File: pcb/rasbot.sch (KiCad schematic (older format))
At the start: 0 parts

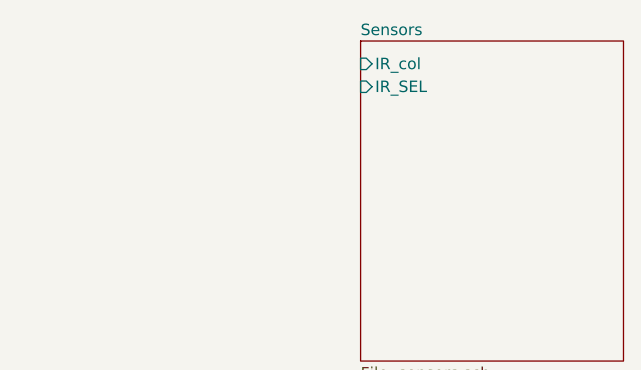
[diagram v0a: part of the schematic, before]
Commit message: IR matrix complete minus control transistor
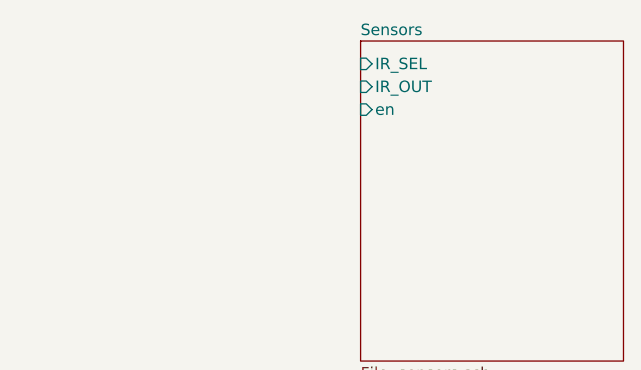
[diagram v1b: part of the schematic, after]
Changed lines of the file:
@@
 $Descr A4 11693 8268
 encoding utf-8
-Sheet 1 19
+Sheet 1 12
 Title ""
 Date ""
@@
 F0 "Sensors" 50
 F1 "sensors.sch" 50
-F2 "IR_col" I L 9200 1300 50
-F3 "IR_SEL" I L 9200 1400 50
+F2 "IR_SEL" I L 9200 1300 50
+F3 "IR_OUT" I L 9200 1400 50
+F4 "en" I L 9200 1500 50
 $EndSheet
 $Sheet

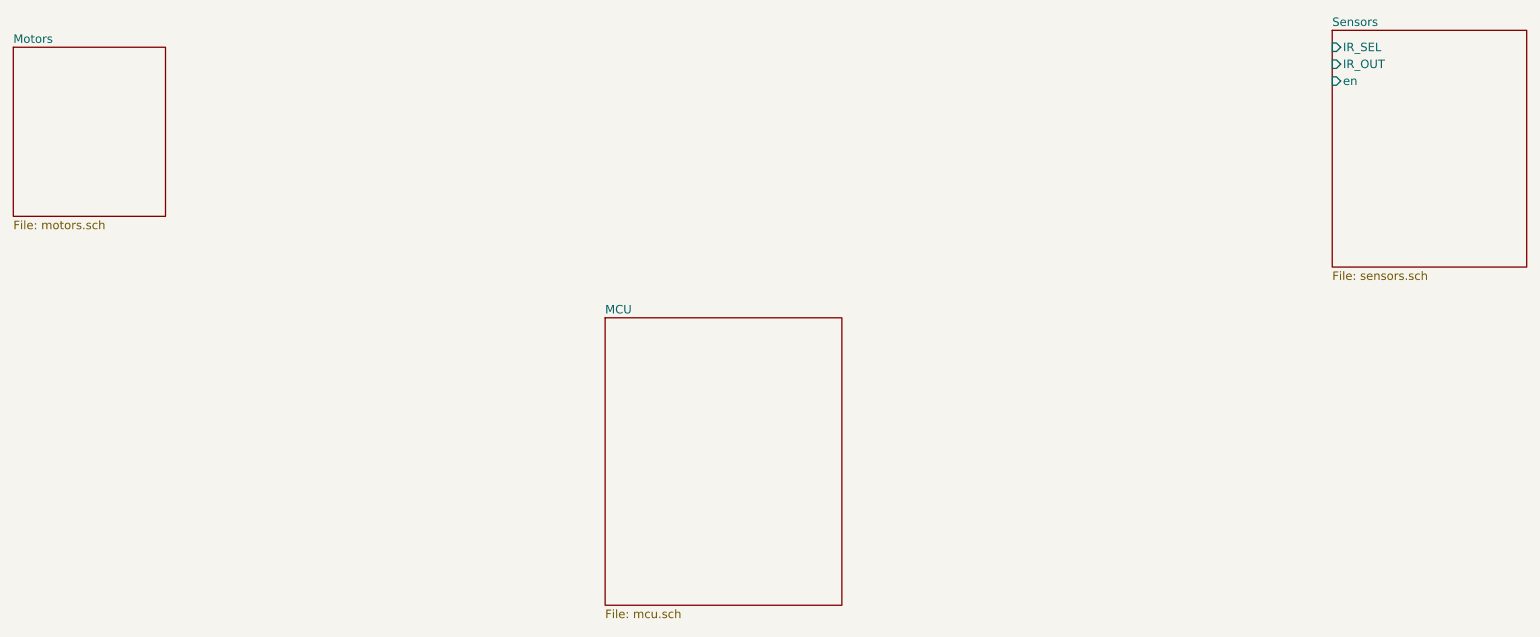
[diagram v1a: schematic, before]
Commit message: Connect IR Matrix to MCU
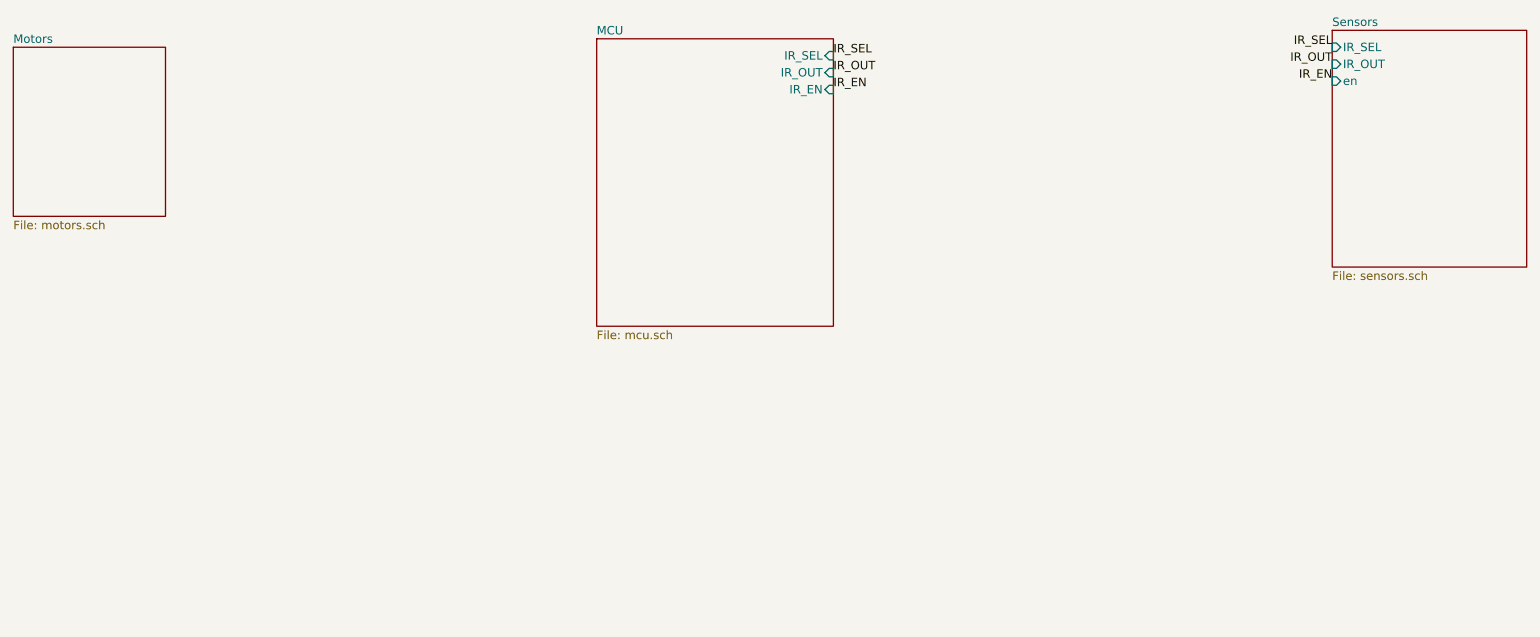
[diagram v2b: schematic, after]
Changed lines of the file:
@@
 $EndDescr
 $Sheet
-S 4900 2900 1400 1700
+S 4850 1250 1400 1700
 U 5D0ADCD4
 F0 "MCU" 50
 F1 "mcu.sch" 50
+F2 "IR_SEL" I R 6250 1350 50
+F3 "IR_OUT" I R 6250 1450 50
+F4 "IR_EN" I R 6250 1550 50
 $EndSheet
 $Sheet
@@
 F1 "motors.sch" 50
 $EndSheet
+Text Label 6250 1350 0    50   ~ 0
+IR_SEL
+Text Label 9200 1300 2    50   ~ 0
+IR_SEL
+Text Label 9200 1400 2    50   ~ 0
+IR_OUT
+Text Label 6250 1450 0    50   ~ 0
+IR_OUT
+Text Label 9200 1500 2    50   ~ 0
+IR_EN
+Text Label 6250 1550 0    50   ~ 0
+IR_EN
 $EndSCHEMATC
